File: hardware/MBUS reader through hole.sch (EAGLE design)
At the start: 17 parts, among them Q1 BC337, Q2 BC337, T1 BC307

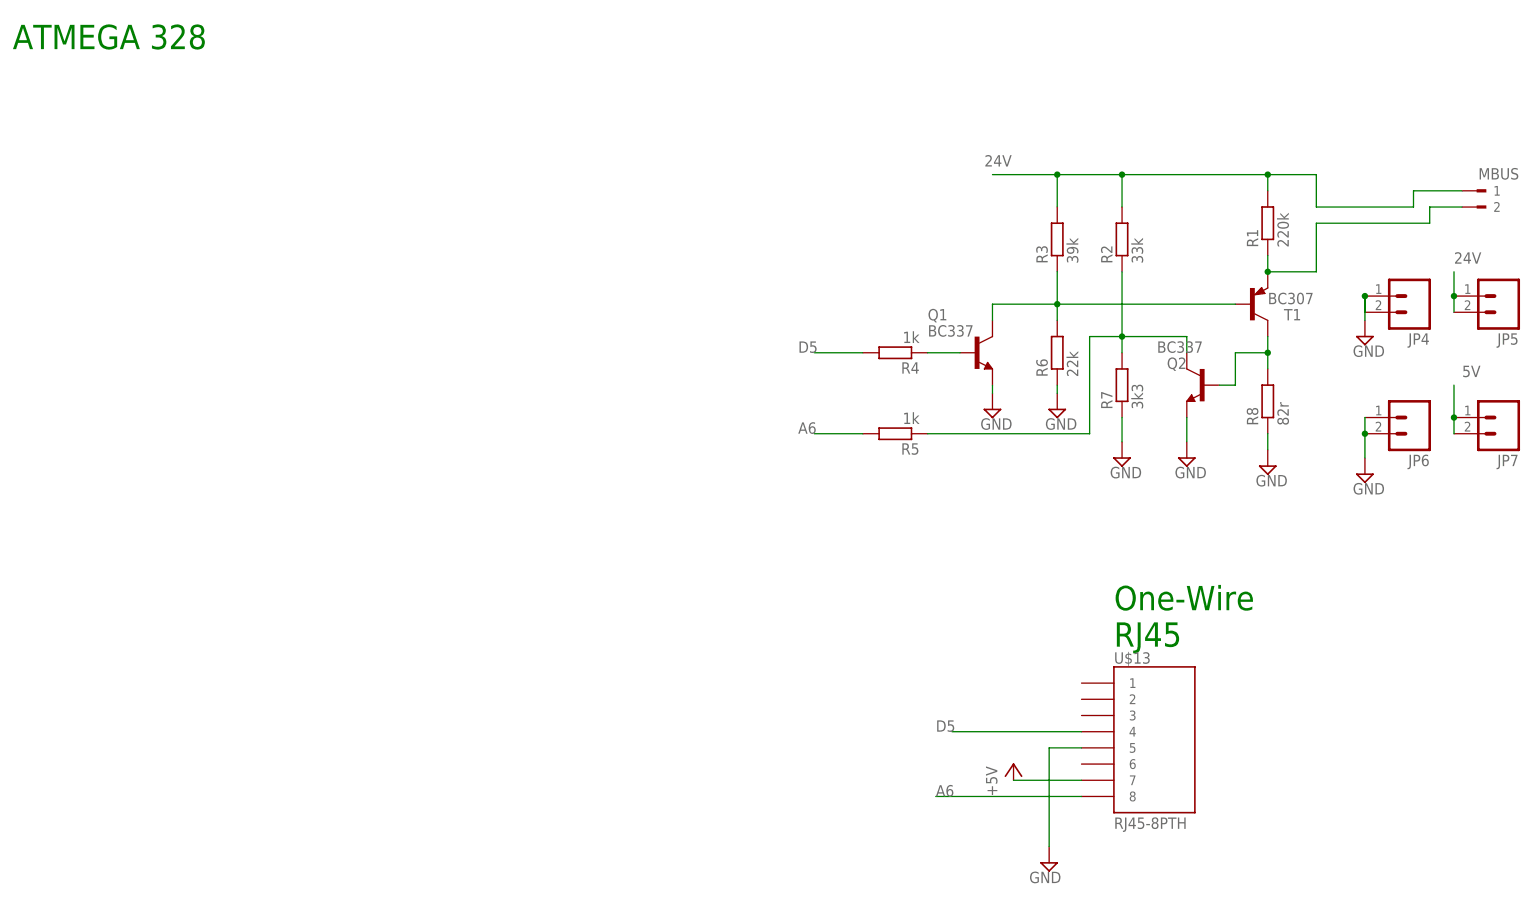
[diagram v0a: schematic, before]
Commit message: through hole with connector blocks
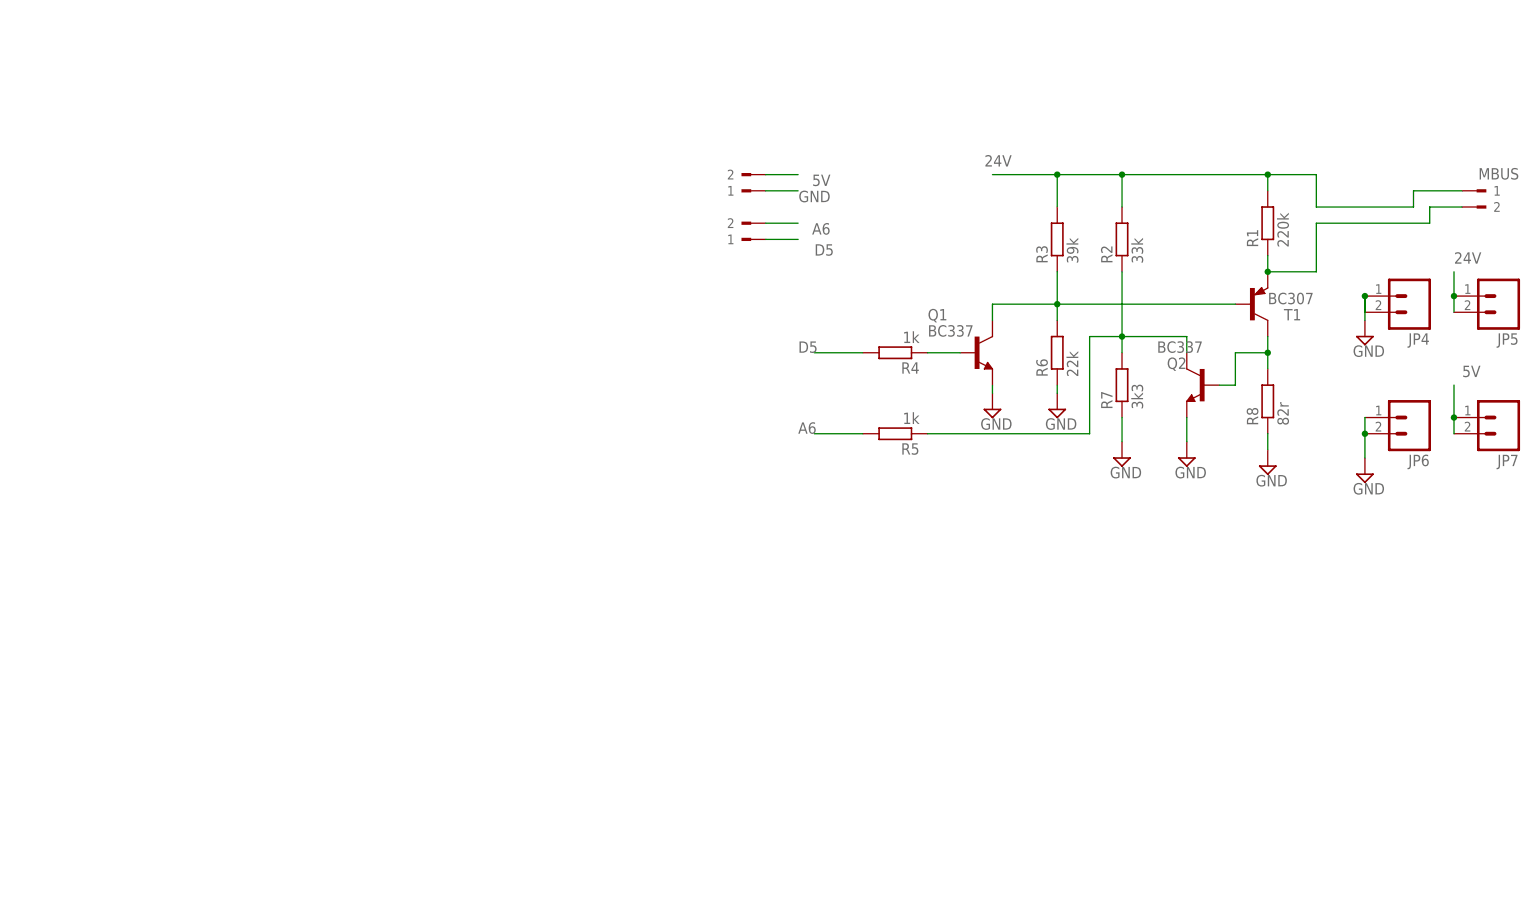
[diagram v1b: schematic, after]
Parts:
- removed U$13: RJ45-8PTH, SparkFun-Connectors:RJ45-8PTH
- added MBUS1, MBUS2: (no value), con-weidmueller-sl35:180-2
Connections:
- net 5V: now also MBUS2.2; no longer U$13.7
- net A6: now also MBUS1.2; no longer U$13.8
- net D5: now also MBUS1.1; no longer U$13.4
- net GND: now also MBUS2.1; no longer U$13.5
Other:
- note removed: "ATMEGA 328"
- note removed: "One-Wire RJ45"
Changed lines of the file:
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@@
 <part name="SUPPLY16" library="supply2" deviceset="GND" device=""/>
 <part name="MBUS" library="con-weidmueller-sl35" library_urn="urn:adsk.eagle:library:199" deviceset="180-2" device=""/>
-<part name="U$13" library="SparkFun-Connectors" deviceset="RJ45-8" device="PTH"/>
-<part name="SUPPLY1" library="supply2" deviceset="GND" device=""/>
-<part name="P+9" library="supply1" deviceset="+5V" device=""/>
+<part name="MBUS1" library="con-weidmueller-sl35" library_urn="urn:adsk.eagle:library:199" deviceset="180-2" device=""/>
+<part name="MBUS2" library="con-weidmueller-sl35" library_urn="urn:adsk.eagle:library:199" deviceset="180-2" device=""/>
 </parts>
 <sheets>
 <sheet>
 <plain>
-<text x="3.81" y="100.965" size="3.81" layer="91">ATMEGA 328</text>
-<text x="176.53" y="7.239" size="3.81" layer="91">One-Wire
-RJ45</text>
 </plain>
 <instances>
@@
 <instance part="SUPPLY16" gate="GND" x="215.9" y="34.29"/>
 <instance part="MBUS" gate="G$1" x="233.68" y="78.74"/>
-<instance part="U$13" gate="G$1" x="184.15" y="-8.636"/>
-<instance part="SUPPLY1" gate="GND" x="166.37" y="-26.67" rot="MR0"/>
-<instance part="P+9" gate="1" x="160.782" y="-11.176"/>
+<instance part="MBUS1" gate="G$1" x="119.38" y="71.12" smashed="yes" rot="R180">
+<attribute name="VALUE" x="119.38" y="76.962" size="1.778" layer="96" rot="R180"/>
+</instance>
+<instance part="MBUS2" gate="G$1" x="119.38" y="78.74" smashed="yes" rot="R180">
+<attribute name="VALUE" x="119.38" y="84.582" size="1.778" layer="96" rot="R180"/>
+</instance>
 </instances>
 <busses>
@@
 </segment>
 <segment>
-<pinref part="U$13" gate="G$1" pin="5"/>
-<wire x1="171.45" y1="-8.636" x2="166.37" y2="-8.636" width="0.1524" layer="91"/>
-<pinref part="SUPPLY1" gate="GND" pin="GND"/>
-<wire x1="166.37" y1="-8.636" x2="166.37" y2="-24.13" width="0.1524" layer="91"/>
+<pinref part="MBUS2" gate="G$1" pin="1"/>
+<wire x1="121.92" y1="78.74" x2="127" y2="78.74" width="0.1524" layer="91"/>
+<label x="132.08" y="78.74" size="1.778" layer="95" rot="R180"/>
 </segment>
 </net>
@@
 </segment>
 <segment>
-<pinref part="U$13" gate="G$1" pin="4"/>
-<wire x1="151.13" y1="-6.096" x2="171.45" y2="-6.096" width="0.1524" layer="91"/>
-<label x="148.59" y="-6.096" size="1.778" layer="95"/>
+<pinref part="MBUS1" gate="G$1" pin="1"/>
+<wire x1="121.92" y1="71.12" x2="127" y2="71.12" width="0.1524" layer="91"/>
+<label x="129.54" y="68.58" size="1.778" layer="95"/>
 </segment>
 </net>
@@
 </segment>
 <segment>
-<pinref part="P+9" gate="1" pin="+5V"/>
-<pinref part="U$13" gate="G$1" pin="7"/>
-<wire x1="160.782" y1="-13.716" x2="171.45" y2="-13.716" width="0.1524" layer="91"/>
+<pinref part="MBUS2" gate="G$1" pin="2"/>
+<wire x1="121.92" y1="81.28" x2="127" y2="81.28" width="0.1524" layer="91"/>
+<label x="132.08" y="81.28" size="1.778" layer="95" rot="R180"/>
 </segment>
 </net>
@@
 <net name="A6" class="0">
 <segment>
-<pinref part="U$13" gate="G$1" pin="8"/>
-<wire x1="171.45" y1="-16.256" x2="148.59" y2="-16.256" width="0.1524" layer="91"/>
-<label x="148.59" y="-16.256" size="1.778" layer="95"/>
-</segment>
-<segment>
 <pinref part="R5" gate="G$1" pin="2"/>
 <wire x1="137.16" y1="40.64" x2="129.54" y2="40.64" width="0.1524" layer="91"/>
 <label x="127" y="40.64" size="1.778" layer="95"/>
+</segment>
+<segment>
+<pinref part="MBUS1" gate="G$1" pin="2"/>
+<wire x1="121.92" y1="73.66" x2="127" y2="73.66" width="0.1524" layer="91"/>
+<label x="132.08" y="73.66" size="1.778" layer="95" rot="R180"/>
 </segment>
 </net>
@@
 </drawing>
 <compatibility>
-<note version="6.3" minversion="6.2.2" severity="warning">
-Since Version 6.2.2 text objects can contain more than one line,
-which will not be processed correctly with this version.
-</note>
 <note version="8.2" severity="warning">
 Since Version 8.2, Eagle supports online libraries. The ids
